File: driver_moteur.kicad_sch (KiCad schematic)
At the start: 28 parts, among them J301 Conn_01x06, J302 Conn_01x06, U301 ZXBM5210-S, U302 ZXBM5210-S

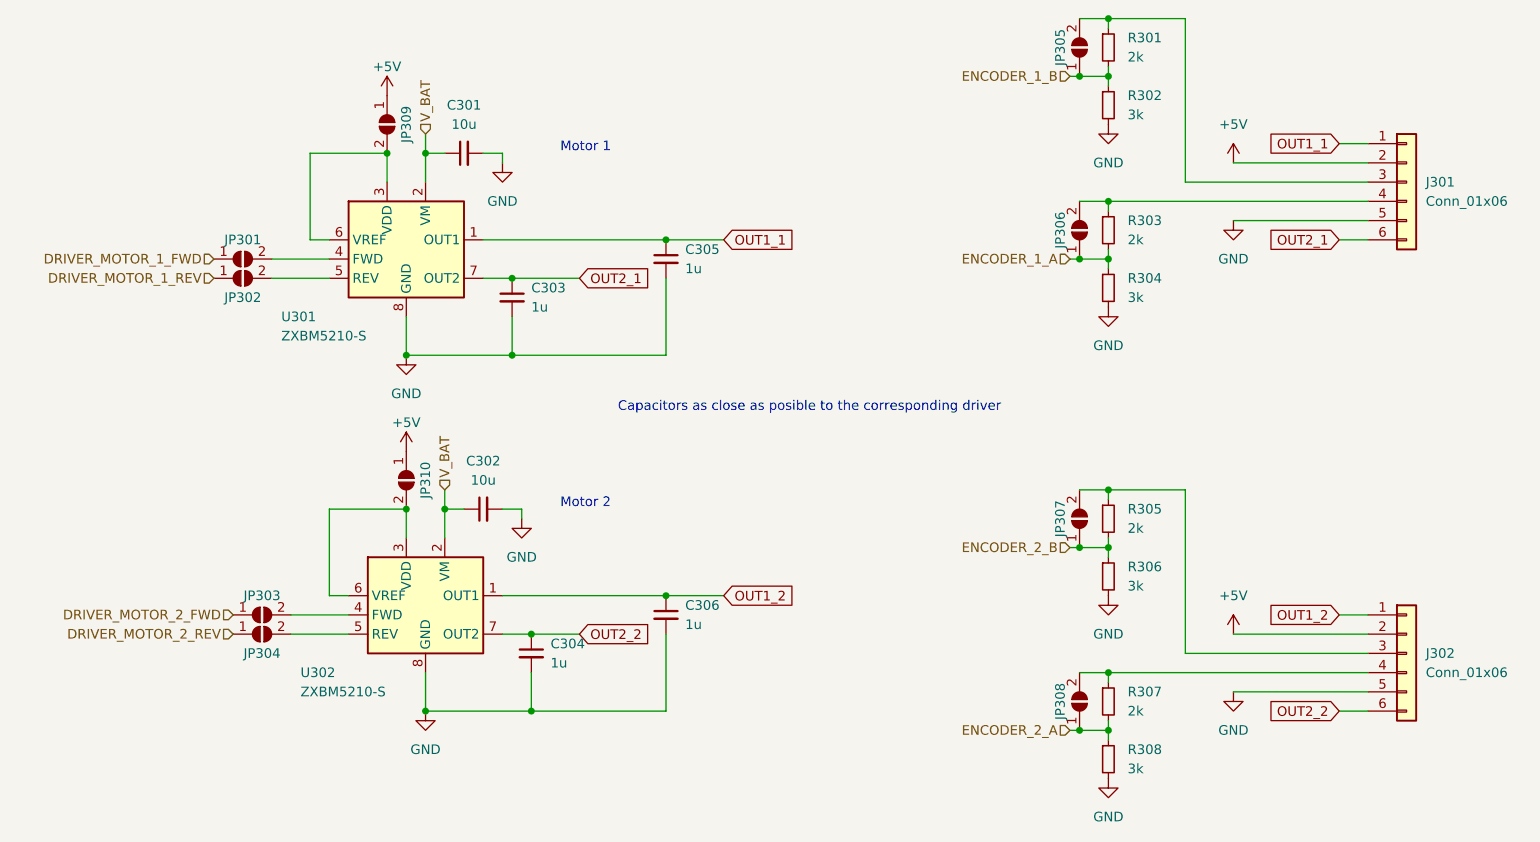
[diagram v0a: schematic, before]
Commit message: I2C bus correction & simplifaction
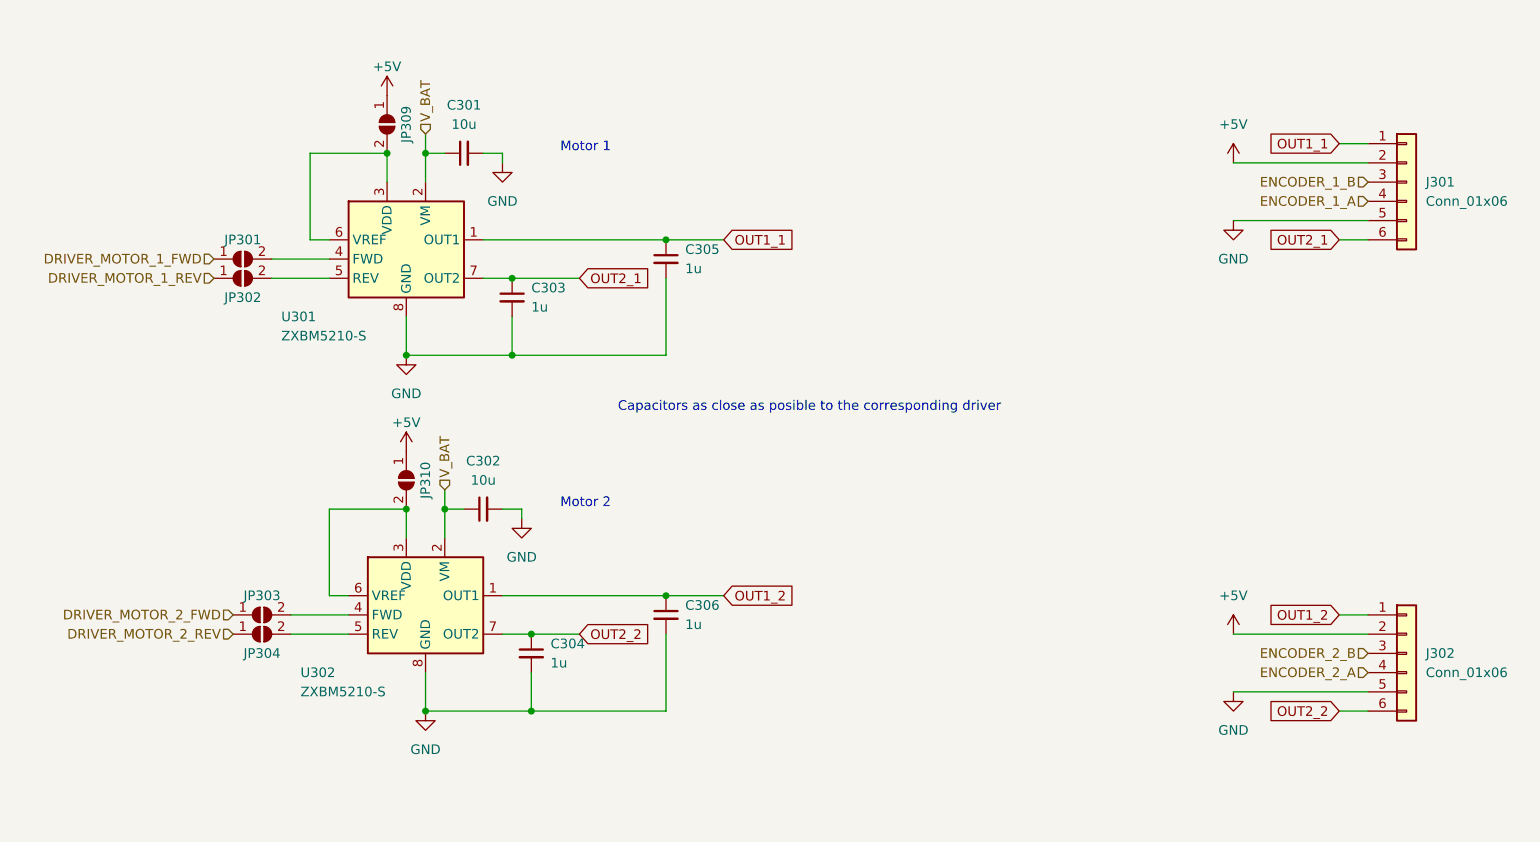
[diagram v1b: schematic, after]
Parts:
- removed JP305, JP306, JP307, JP308: SolderJumper_2_Open, Jumper:SolderJumper-2_P1.3mm_Open_TrianglePad1.0x1.5mm, symbol Jumper:SolderJumper_2_Open
- removed R301, R303, R305, R307: 2k, Resistor_SMD:R_0603_1608Metric_Pad0.98x0.95mm_HandSolder, symbol Device:R_Small
- removed R302, R304, R306, R308: 3k, Resistor_SMD:R_0603_1608Metric_Pad0.98x0.95mm_HandSolder, symbol Device:R_Small
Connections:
- net ENCODER_1_A: now also J301.4 (Pin_4)
- net ENCODER_1_B: now also J301.3 (Pin_3)
- net ENCODER_2_A: now also J302.4 (Pin_4)
- net ENCODER_2_B: now also J302.3 (Pin_3)
